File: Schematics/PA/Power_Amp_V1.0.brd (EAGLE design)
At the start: 50.5 x 77.8 mm, 103 parts, among them J1 4_PIN_AMPCONN, J12 1725724, J13 1725724, J14 1725724, J2 1984633, J3 2TERMINAL_SPEAKER, J4 2TERMINAL_SPEAKER, J5 2TERMINAL_SPEAKER, U1 LME49830, U2 LME49830, U3 LME49830

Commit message: small changes to the PA
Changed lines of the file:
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@@
 <layer number="27" name="tValues" color="7" fill="1" visible="no" active="yes"/>
 <layer number="28" name="bValues" color="7" fill="1" visible="no" active="yes"/>
-<layer number="29" name="tStop" color="7" fill="3" visible="yes" active="yes"/>
-<layer number="30" name="bStop" color="7" fill="6" visible="yes" active="yes"/>
+<layer number="29" name="tStop" color="7" fill="3" visible="no" active="yes"/>
+<layer number="30" name="bStop" color="7" fill="6" visible="no" active="yes"/>
 <layer number="31" name="tCream" color="7" fill="4" visible="no" active="yes"/>
 <layer number="32" name="bCream" color="7" fill="5" visible="no" active="yes"/>
@@
 <wire x1="0" y1="76.5175" x2="0.635" y2="77.1525" width="0" layer="20" curve="-90"/>
 <wire x1="0.635" y1="77.1525" x2="1.27" y2="77.7875" width="0" layer="20" curve="-90"/>
-<text x="46.6725" y="39.37" size="0.889" layer="21" font="vector" ratio="15" rot="R90">Nov, 2015</text>
+<text x="46.955534375" y="39.879403125" size="0.889" layer="21" font="vector" ratio="15" rot="R90">Nov, 2015</text>
 <wire x1="34.6075" y1="5.08" x2="36.5125" y2="5.08" width="2.159" layer="29"/>
 <wire x1="30.48" y1="5.08" x2="34.6075" y2="5.08" width="2.159" layer="30"/>
@@
 </element>
 <element name="C11" library="rcl" package="C050-024X044" value="0.1uF" x="22.352" y="52.832" smashed="yes" rot="R180">
-<attribute name="NAME" x="17.8435" y="53.34" size="0.889" layer="25" font="vector" ratio="15" rot="R180"/>
+<attribute name="NAME" x="24.382" y="55.00970625" size="0.889" layer="25" font="vector" ratio="15" rot="R180"/>
 <attribute name="VALUE" x="24.511" y="55.499" size="1.27" layer="27" ratio="10" rot="R180"/>
 </element>
@@
 </element>
 <element name="C15" library="rcl" package="C050-024X044" value="0.1uF" x="45.6565" y="56.007" smashed="yes" rot="R90">
-<attribute name="NAME" x="42.147246875" y="53.897678125" size="0.889" layer="25" font="vector" ratio="15"/>
+<attribute name="NAME" x="44.14573125" y="54.511896875" size="0.889" layer="25" font="vector" ratio="15" rot="R90"/>
 <attribute name="VALUE" x="48.3235" y="53.848" size="1.27" layer="27" ratio="10" rot="R90"/>
 </element>
 <element name="C16" library="rcl" package="E2,5-6" value="100uF" x="20.6375" y="41.91" smashed="yes" rot="R270">
-<attribute name="NAME" x="18.288" y="44.831" size="0.889" layer="25" font="vector" ratio="15" rot="R180"/>
+<attribute name="NAME" x="18.231390625" y="44.2367" size="0.889" layer="25" font="vector" ratio="15" rot="R180"/>
 <attribute name="VALUE" x="17.9705" y="39.243" size="1.27" layer="27" ratio="10" rot="R270"/>
 </element>
@@
 <element name="J1" library="Amplifier_Parts" package="4_PIN_AMPCON" value="4_PIN_AMPCONN" x="5.3975" y="4.445" smashed="yes" rot="R180"/>
 <element name="PR1" library="rcl" package="0617V" value="" x="39.0525" y="41.5925" smashed="yes" rot="R270">
-<attribute name="NAME" x="42.4424875" y="44.68348125" size="0.889" layer="25" font="vector" ratio="15"/>
+<attribute name="NAME" x="42.15945" y="45.617384375" size="0.889" layer="25" font="vector" ratio="15"/>
 <attribute name="VALUE" x="36.4363" y="40.9575" size="1.27" layer="27" ratio="10" rot="R270"/>
 </element>
@@
 </element>
 <element name="R45" library="rcl" package="0204V" value="500" x="20.1295" y="56.515" smashed="yes">
-<attribute name="NAME" x="15.721065625" y="55.539609375" size="0.889" layer="25" font="vector" ratio="15"/>
+<attribute name="NAME" x="19.242728125" y="54.95246875" size="0.889" layer="25" font="vector" ratio="15"/>
 <attribute name="VALUE" x="17.9959" y="54.2036" size="1.27" layer="27" ratio="10"/>
 </element>
@@
 </element>
 <element name="R47" library="rcl" package="0204V" value="1.2k" x="26.0985" y="66.8655" smashed="yes" rot="R180">
-<attribute name="NAME" x="30.895309375" y="67.3754625" size="0.889" layer="25" font="vector" ratio="15" rot="R180"/>
+<attribute name="NAME" x="27.274390625" y="65.81009375" size="0.889" layer="25" font="vector" ratio="15" rot="R180"/>
 <attribute name="VALUE" x="28.2321" y="69.1769" size="1.27" layer="27" ratio="10" rot="R180"/>
 </element>
@@
 </element>
 <element name="R51" library="rcl" package="0309V" value="10" x="44.323" y="61.214" smashed="yes" rot="R180">
-<attribute name="NAME" x="43.448309375" y="59.838809375" size="0.889" layer="25" font="vector" ratio="15" rot="R270"/>
+<attribute name="NAME" x="43.154721875" y="60.3279875" size="0.889" layer="25" font="vector" ratio="15" rot="R270"/>
 <attribute name="VALUE" x="44.069" y="63.4238" size="1.27" layer="27" ratio="10" rot="R180"/>
 </element>
@@
 </element>
 <element name="R9" library="rcl" package="0204V" value="4.7k" x="17.145" y="48.26" smashed="yes" rot="R270">
-<attribute name="NAME" x="15.6464" y="50.3809" size="0.889" layer="25" font="vector" ratio="15"/>
+<attribute name="NAME" x="16.382334375" y="45.4000875" size="0.889" layer="25" font="vector" ratio="15"/>
 <attribute name="VALUE" x="14.8336" y="50.3936" size="1.27" layer="27" ratio="10" rot="R270"/>
 </element>
@@
 <wire x1="36.83" y1="28.8925" x2="36.83" y2="30.7975" width="2.032" layer="1"/>
 <wire x1="36.83" y1="30.7975" x2="37.465" y2="31.4325" width="2.032" layer="1"/>
-<wire x1="46.355" y1="33.3375" x2="48.621853125" y2="35.569815625" width="2.032" layer="1"/>
 <wire x1="29.845" y1="27.6225" x2="30.7975" y2="27.6225" width="2.032" layer="16"/>
 <wire x1="30.7975" y1="27.6225" x2="31.75" y2="28.575" width="2.032" layer="16"/>
@@
 <wire x1="37.465" y1="31.4325" x2="41.5925" y2="31.4325" width="2.032" layer="1"/>
 <wire x1="41.5925" y1="31.4325" x2="43.4975" y2="33.3375" width="2.032" layer="1"/>
-<wire x1="43.4975" y1="33.3375" x2="46.355" y2="33.3375" width="2.032" layer="1"/>
-<wire x1="48.5775" y1="57.4675" x2="48.5775" y2="9.8841125" width="2.032" layer="1"/>
+<wire x1="43.4975" y1="33.3375" x2="47.0405625" y2="33.3375" width="2.032" layer="1"/>
+<wire x1="48.5775" y1="57.4675" x2="48.5775" y2="34.8744375" width="2.032" layer="1"/>
+<wire x1="48.5775" y1="34.8744375" x2="48.5775" y2="9.8841125" width="2.032" layer="1"/>
 <wire x1="48.5775" y1="9.8841125" x2="48.41105625" y2="9.71766875" width="2.032" layer="1"/>
-<wire x1="9.8425" y1="8.255" x2="12.065" y2="26.035" width="0" layer="19" extent="16-16"/>
+<wire x1="47.0405625" y1="33.3375" x2="48.5775" y2="34.8744375" width="2.032" layer="1"/>
 </signal>
 <signal name="RIGHT_IN">

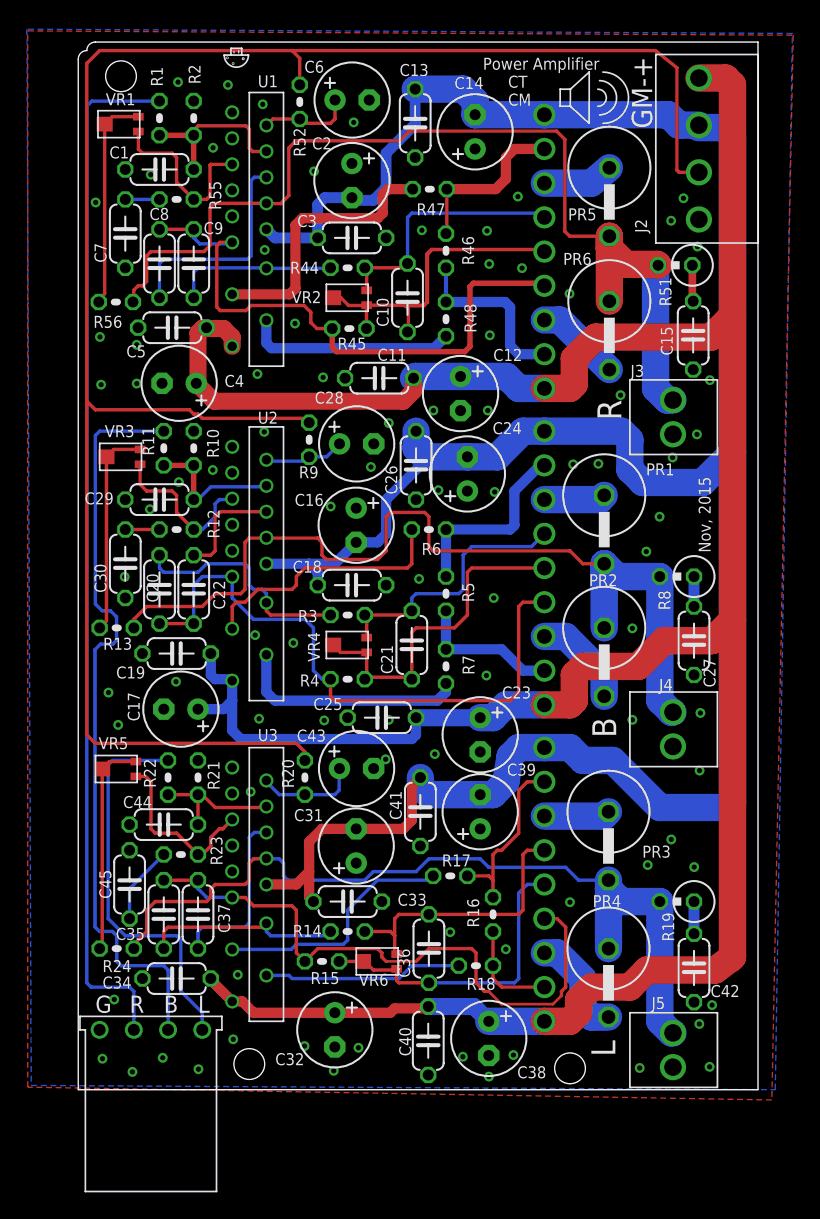
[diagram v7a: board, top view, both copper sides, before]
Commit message: changes holes to #4 size
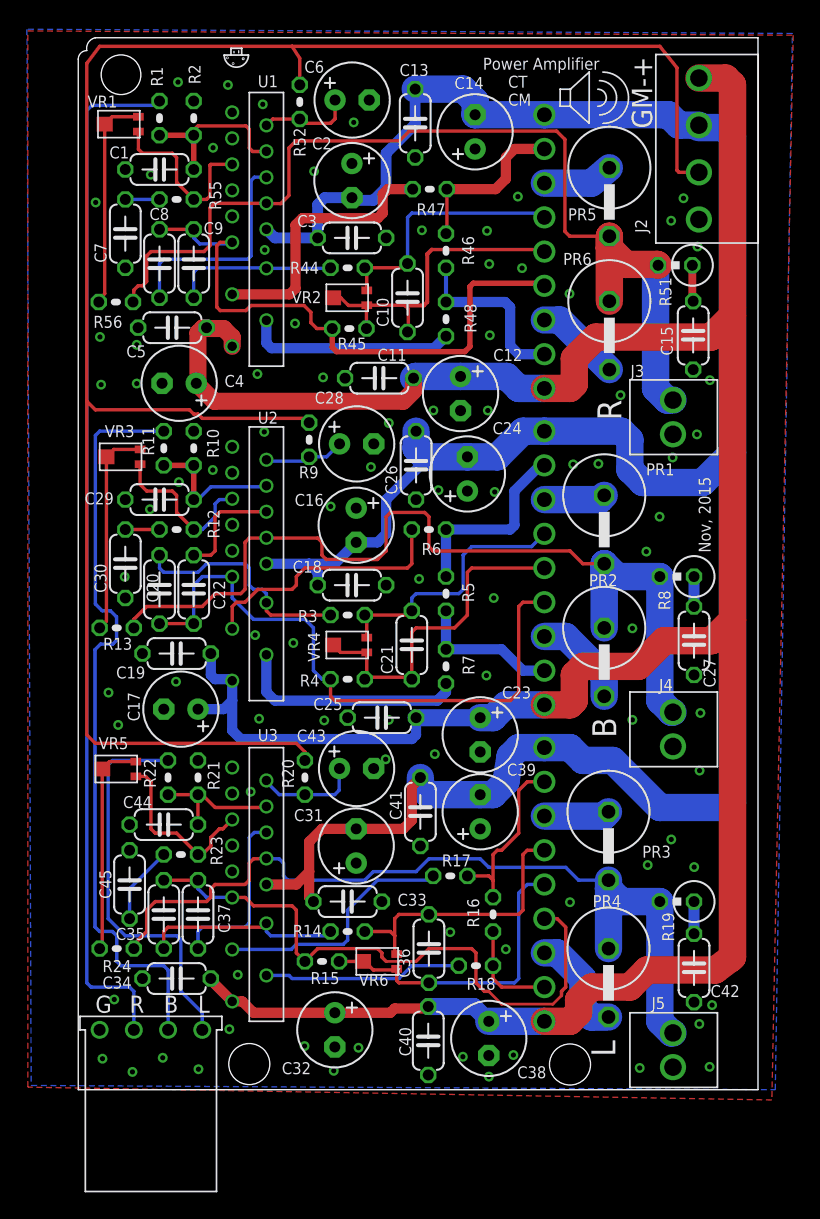
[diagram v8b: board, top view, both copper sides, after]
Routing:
- net MUTE: track 141.1 -> 141.9 mm
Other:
- board size 50.5 x 77.8 mm -> 50.5 x 78.1 mm
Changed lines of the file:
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@@
 <setting verticaltext="up"/>
 </settings>
-<grid distance="0.003125" unitdist="mic" unit="inch" style="lines" multiple="1" display="yes" altdistance="0.025" altunitdist="inch" altunit="inch"/>
+<grid distance="0.0125" unitdist="inch" unit="inch" style="lines" multiple="1" display="yes" altdistance="0.025" altunitdist="inch" altunit="inch"/>
 <layers>
 <layer number="1" name="Top" color="4" fill="1" visible="yes" active="yes"/>
@@
 <plain>
 <wire x1="0" y1="0" x2="50.47" y2="0" width="0" layer="20"/>
-<wire x1="50.47" y1="0" x2="50.47" y2="77.7875" width="0" layer="20"/>
-<wire x1="50.47" y1="77.7875" x2="1.27" y2="77.7875" width="0" layer="20"/>
+<wire x1="50.47" y1="0" x2="50.47" y2="78.105" width="0" layer="20"/>
+<wire x1="50.47" y1="78.105" x2="1.27" y2="78.105" width="0" layer="20"/>
 <wire x1="0" y1="76.5175" x2="0" y2="0" width="0" layer="20"/>
 <text x="30.043725" y="75.73103125" size="0.889" layer="21" font="vector" ratio="15">Power Amplifier</text>
@@
 <text x="6.35" y="5.715" size="1.27" layer="21" font="vector" ratio="15">B</text>
 <text x="8.89" y="5.715" size="1.27" layer="21" font="vector" ratio="15">L</text>
-<hole x="12.7" y="1.905" drill="2.286"/>
-<hole x="36.5125" y="1.5875" drill="2.286"/>
-<hole x="3.175" y="75.2475" drill="2.286"/>
+<hole x="12.7" y="1.905" drill="3.048"/>
+<hole x="36.5125" y="1.872828125" drill="3.048"/>
+<hole x="3.175" y="75.3607" drill="2.9464"/>
 <wire x1="0" y1="76.5175" x2="0.635" y2="77.1525" width="0" layer="20" curve="-90"/>
-<wire x1="0.635" y1="77.1525" x2="1.27" y2="77.7875" width="0" layer="20" curve="-90"/>
+<wire x1="0.635" y1="77.1525" x2="1.27" y2="78.105" width="0" layer="20" curve="-90"/>
 <text x="46.955534375" y="39.879403125" size="0.889" layer="21" font="vector" ratio="15" rot="R90">Nov, 2015</text>
 <wire x1="34.6075" y1="5.08" x2="36.5125" y2="5.08" width="2.159" layer="29"/>
@@
 </element>
 <element name="C32" library="rcl" package="E2,5-6" value="100uF" x="19.05" y="4.445" smashed="yes" rot="R270">
-<attribute name="NAME" x="14.62535625" y="1.821434375" size="0.889" layer="25" font="vector" ratio="15"/>
+<attribute name="NAME" x="15.11653125" y="1.15299375" size="0.889" layer="25" font="vector" ratio="15"/>
 <attribute name="VALUE" x="16.383" y="1.778" size="1.27" layer="27" ratio="10" rot="R270"/>
 </element>
@@
 </element>
 <element name="VR1" library="Amplifier_Parts" package="EVM2W" value="" x="3.3655" y="71.6915" smashed="yes" rot="R90">
-<attribute name="NAME" x="2.0409125" y="73.09325" size="0.889" layer="25" font="vector" ratio="15"/>
+<attribute name="NAME" x="0.6821" y="72.923446875" size="0.889" layer="25" font="vector" ratio="15"/>
 </element>
 <element name="VR2" library="Amplifier_Parts" package="EVM2W" value="" x="20.32" y="58.801" smashed="yes" rot="R90">
@@
 <via x="41.144353125" y="27.460778125" extent="1-16" drill="0.381"/>
 <via x="6.274053125" y="2.371746875" extent="1-16" drill="0.381"/>
-<via x="11.50751875" y="3.7418" extent="1-16" drill="0.381"/>
+<via x="11.220996875" y="4.492090625" extent="1-16" drill="0.381"/>
 <via x="4.0236625" y="1.323234375" extent="1-16" drill="0.381"/>
 <via x="8.924515625" y="1.523334375" extent="1-16" drill="0.381"/>
@@
 <contactref element="R1" pad="2"/>
 <contactref element="J1" pad="1"/>
-<wire x1="6.0325" y1="73.406" x2="1.016" y2="73.406" width="0.254" layer="16"/>
-<wire x1="1.016" y1="73.406" x2="0.635" y2="73.025" width="0.254" layer="16"/>
-<wire x1="0.635" y1="73.025" x2="0.635" y2="7.9375" width="0.254" layer="16"/>
+<wire x1="1.016" y1="73.0885" x2="0.635" y2="72.7075" width="0.254" layer="16"/>
+<wire x1="0.635" y1="72.7075" x2="0.635" y2="7.9375" width="0.254" layer="16"/>
 <wire x1="0.635" y1="7.9375" x2="0.9525" y2="7.62" width="0.254" layer="16"/>
 <wire x1="0.9525" y1="7.62" x2="3.81" y2="7.62" width="0.254" layer="16"/>
 <wire x1="3.81" y1="7.62" x2="4.1275" y2="7.3025" width="0.254" layer="16"/>
 <wire x1="4.1275" y1="7.3025" x2="4.1275" y2="4.445" width="0.254" layer="16"/>
+<wire x1="1.016" y1="73.0885" x2="5.715" y2="73.0885" width="0.254" layer="16"/>
+<wire x1="5.715" y1="73.0885" x2="6.0325" y2="73.406" width="0.254" layer="16"/>
 </signal>
 <signal name="MUTE">
@@
 <wire x1="44.5975" y1="68.115" x2="44.45" y2="68.2625" width="0.254" layer="1"/>
 <wire x1="44.45" y1="68.2625" x2="44.45" y2="75.8825" width="0.254" layer="1"/>
-<wire x1="44.45" y1="75.8825" x2="42.8625" y2="77.1525" width="0.254" layer="1"/>
+<wire x1="44.45" y1="75.8825" x2="43.18" y2="77.47" width="0.254" layer="1"/>
 <wire x1="0.635" y1="76.2" x2="0.635" y2="51.1175" width="0.254" layer="1"/>
 <wire x1="9.2075" y1="49.8475" x2="8.89" y2="50.165" width="0.254" layer="1"/>
@@
 <wire x1="16.8275" y1="25.0825" x2="16.1925" y2="25.7175" width="0.254" layer="1"/>
 <wire x1="16.1925" y1="25.7175" x2="1.27" y2="25.7175" width="0.254" layer="1"/>
-<wire x1="1.5875" y1="77.1525" x2="0.635" y2="76.2" width="0.254" layer="1"/>
-<wire x1="42.8625" y1="77.1525" x2="15.875" y2="77.1525" width="0.254" layer="1"/>
-<wire x1="15.875" y1="77.1525" x2="1.5875" y2="77.1525" width="0.254" layer="1"/>
+<wire x1="1.5875" y1="77.47" x2="0.635" y2="76.2" width="0.254" layer="1"/>
+<wire x1="43.18" y1="77.47" x2="15.875" y2="77.47" width="0.254" layer="1"/>
+<wire x1="15.875" y1="77.47" x2="1.5875" y2="77.47" width="0.254" layer="1"/>
 <wire x1="16.4465" y1="74.6125" x2="16.4465" y2="76.581" width="0.254" layer="1"/>
-<wire x1="16.4465" y1="76.581" x2="15.875" y2="77.1525" width="0.254" layer="1"/>
+<wire x1="16.4465" y1="76.581" x2="15.875" y2="77.47" width="0.254" layer="1"/>
 </signal>
 <signal name="LEFT_IN">
